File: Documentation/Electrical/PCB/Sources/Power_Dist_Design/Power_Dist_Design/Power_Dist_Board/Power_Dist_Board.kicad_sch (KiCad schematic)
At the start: 59 parts, among them J1 Battery Connector, J2 5V_Power_Rail, J3 5V_Power_Rail, J4 3.3V_Power_Rail, J5 3.3V_Power_Rail, J6 GND_Rail, J7 GND_Rail, M1 Motor_DC, M10 Motor_DC, M2 Motor_DC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

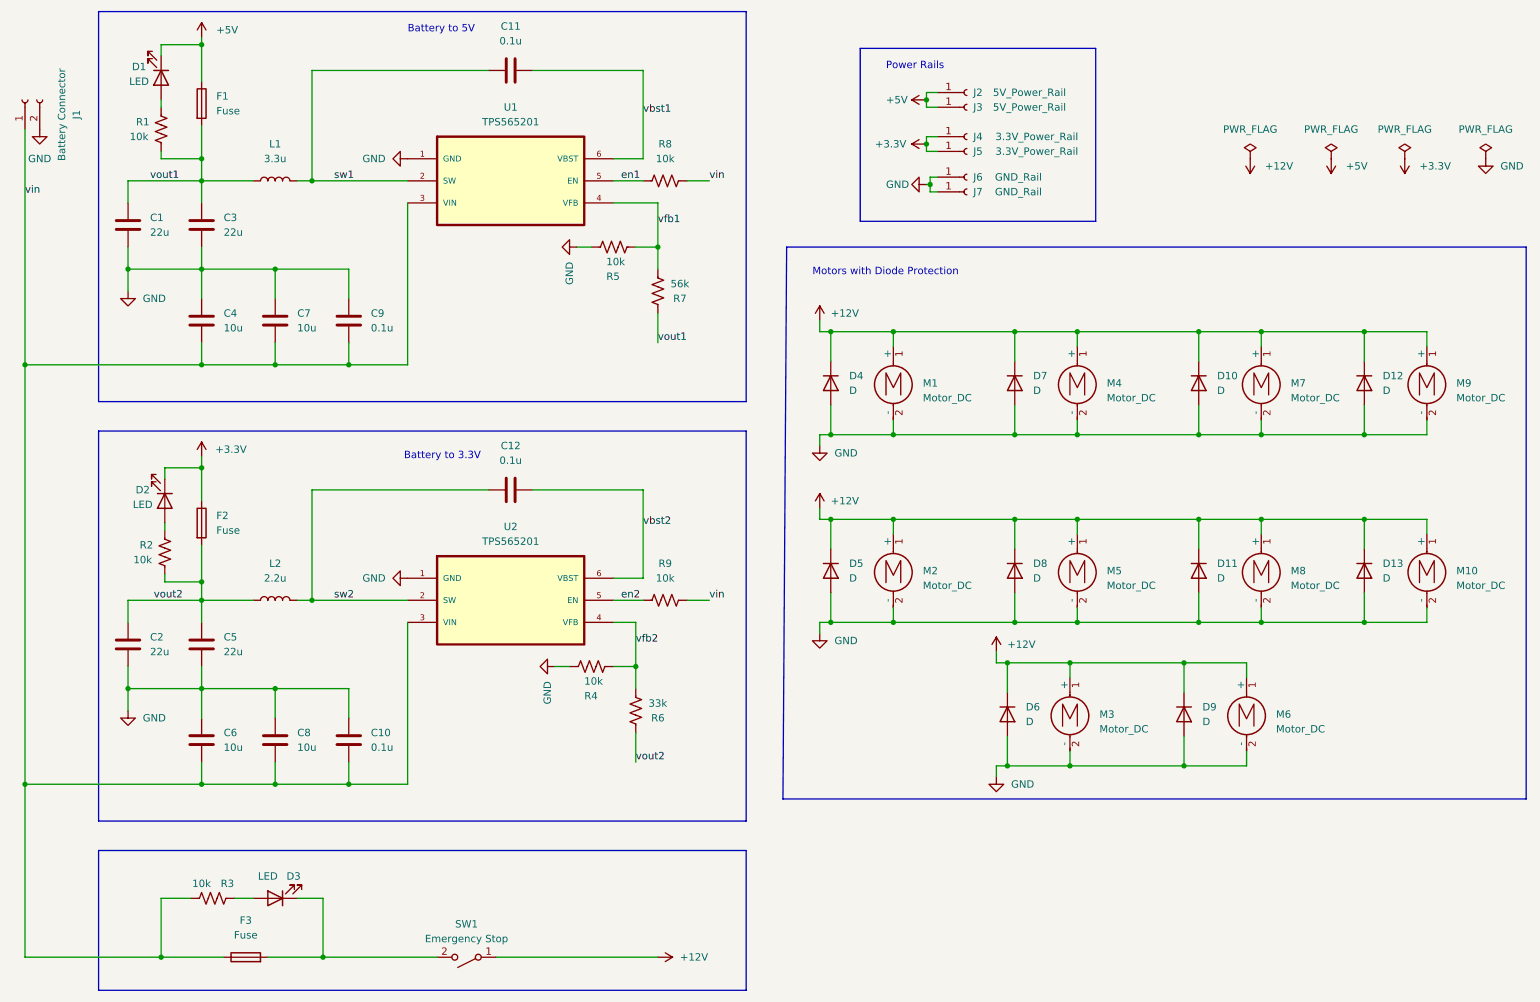
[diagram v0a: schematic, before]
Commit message: Changed ground plane and added jumpers to motor-ground and ground connection
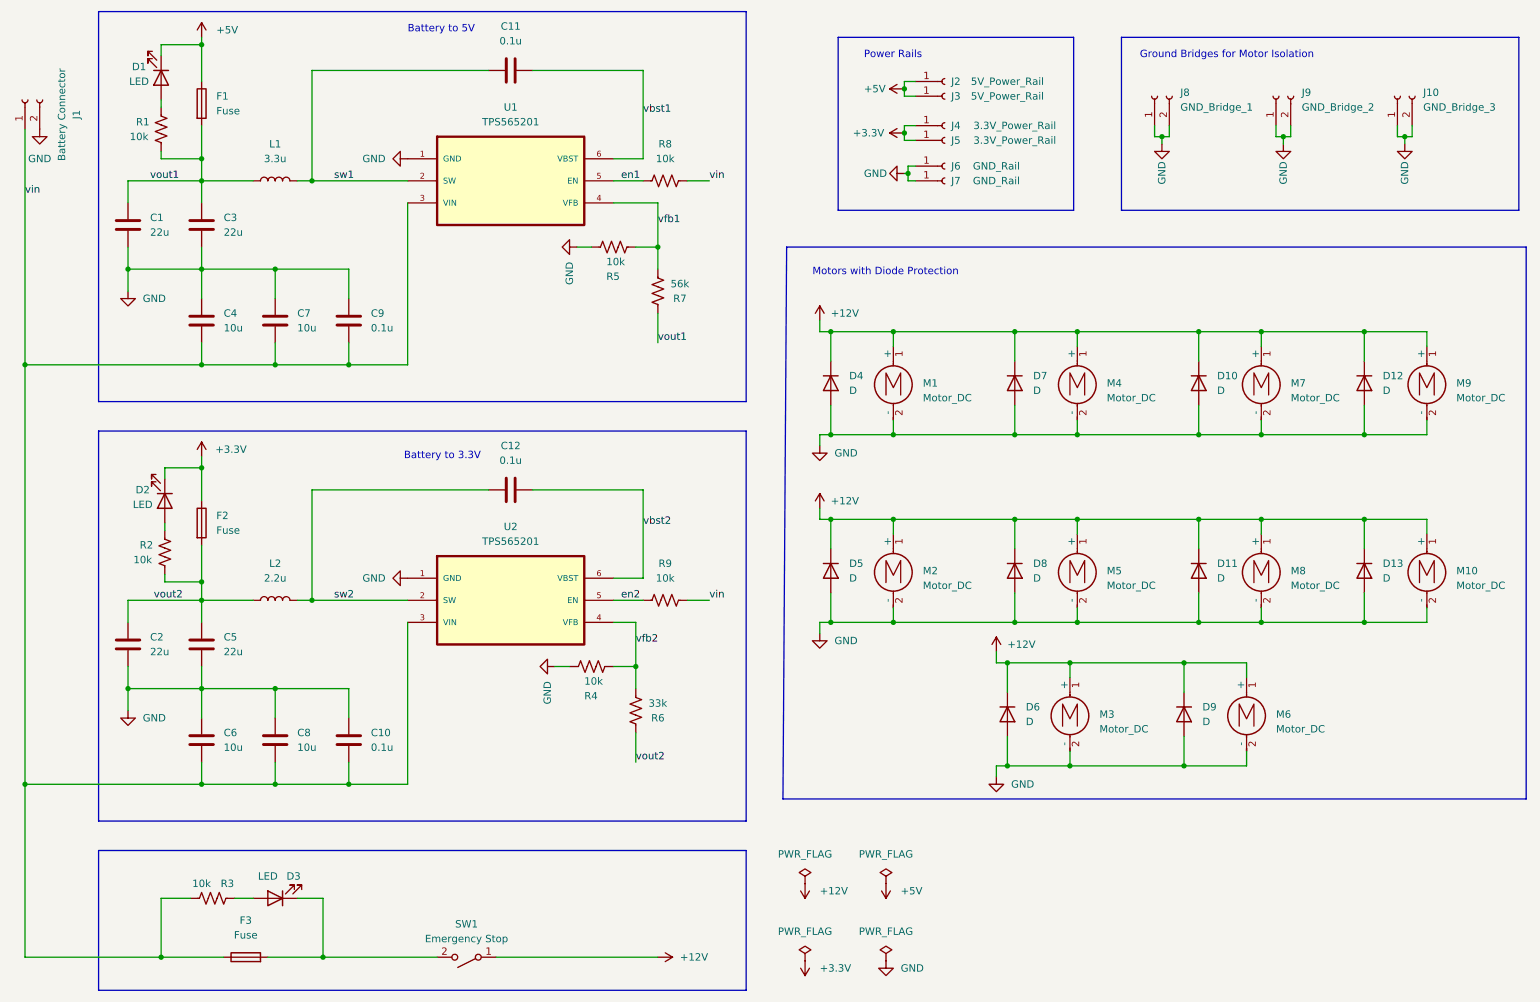
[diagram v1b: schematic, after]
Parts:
- added J10: GND_Bridge_3, Power_Dist:GND_Bridge, symbol Connector:Conn_01x02_Socket
- added J8: GND_Bridge_1, Power_Dist:GND_Bridge, symbol Connector:Conn_01x02_Socket
- added J9: GND_Bridge_2, Power_Dist:GND_Bridge, symbol Connector:Conn_01x02_Socket
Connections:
- net GND: now also J10.1 (Pin_1), J10.2 (Pin_2), J8.1 (Pin_1), J8.2 (Pin_2), J9.1 (Pin_1), J9.2 (Pin_2)
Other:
- note added: "Ground Bridges for Motor Isolation"
- moved on the sheet: J2, J3, J4, J5, J6, J7

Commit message: Finalized pcb
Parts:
- L1, L2: footprint Resistor_SMD:R_1206_3216Metric_Pad1.30x1.75mm_HandSolder -> L_TDK_SPM6530:IND_SPM6530_TDK
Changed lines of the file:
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@@
       (effects (font (size 1.27 1.27)))
     )
-    (property "Footprint" "Resistor_SMD:R_1206_3216Metric_Pad1.30x1.75mm_HandSolder" (at 62.23 119.38 0)
+    (property "Footprint" "L_TDK_SPM6530:IND_SPM6530_TDK" (at 62.23 119.38 0)
       (effects (font (size 1.27 1.27)) hide)
     )
@@
       (effects (font (size 1.27 1.27)))
     )
-    (property "Footprint" "Resistor_SMD:R_1206_3216Metric_Pad1.30x1.75mm_HandSolder" (at 62.23 46.99 0)
-      (effects (font (size 1.27 1.27)) hide)
-    )
+    (property "Footprint" "L_TDK_SPM6530:IND_SPM6530_TDK" (at 62.23 46.99 0)
+      (effects (font (size 1.27 1.27)) hide)
+    )
